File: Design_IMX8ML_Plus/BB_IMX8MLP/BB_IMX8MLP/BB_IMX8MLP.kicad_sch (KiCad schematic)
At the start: 0 parts

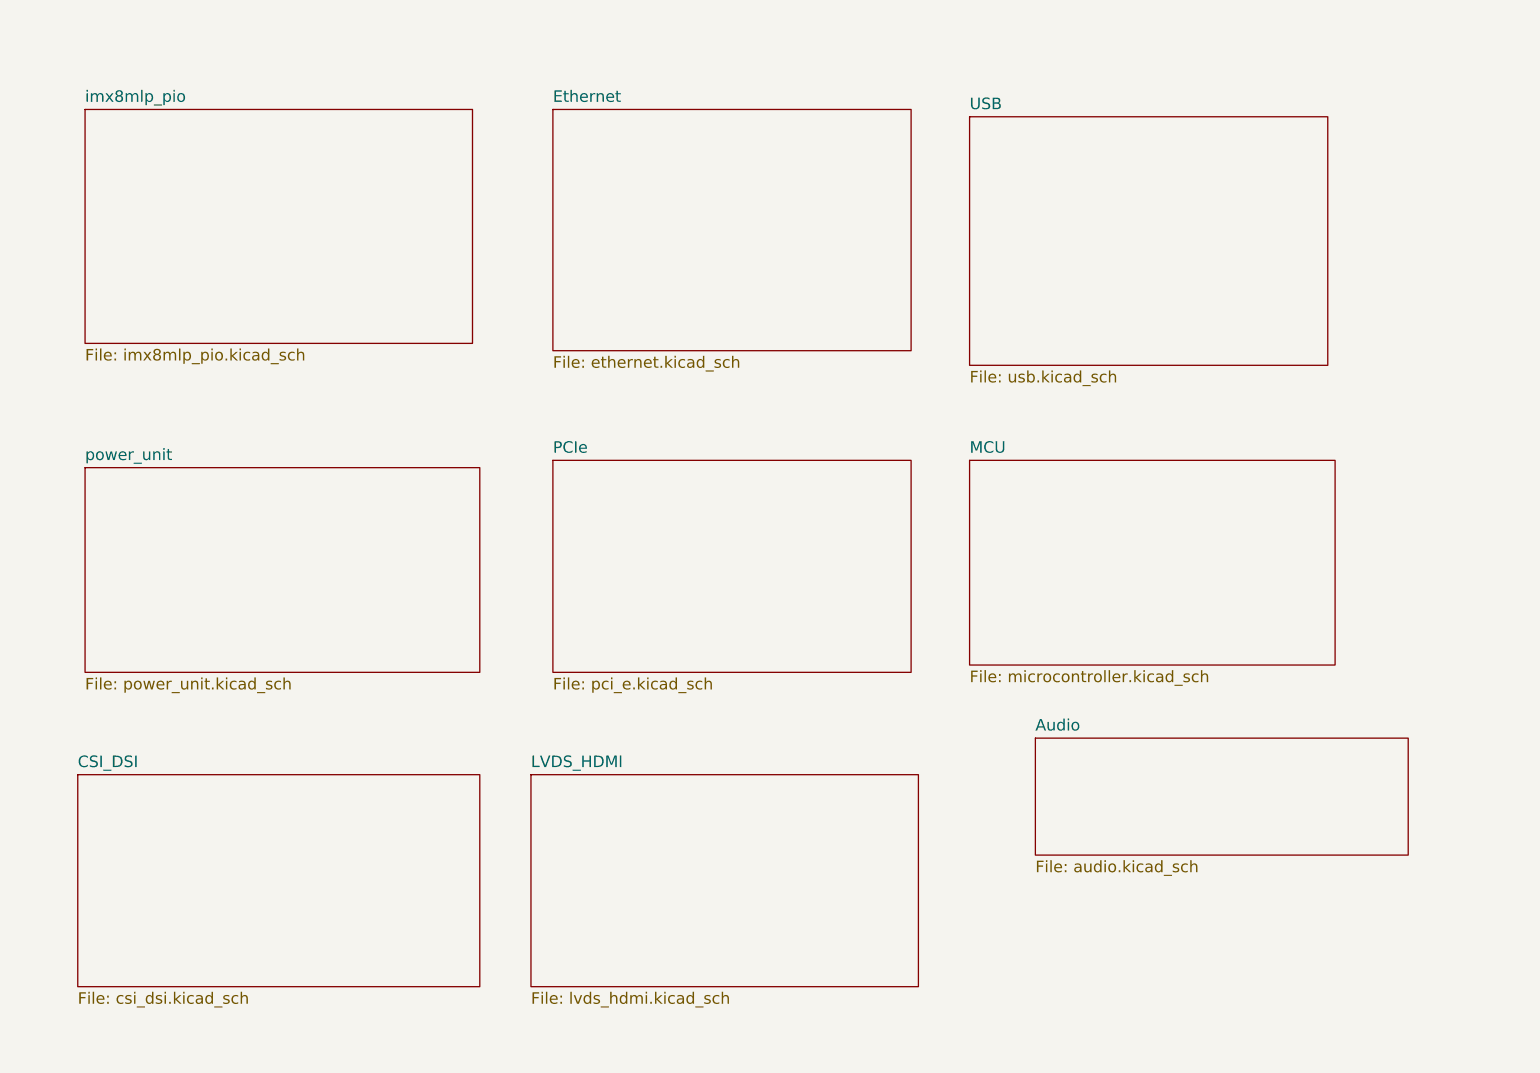
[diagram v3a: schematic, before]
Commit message: Adds audio interface
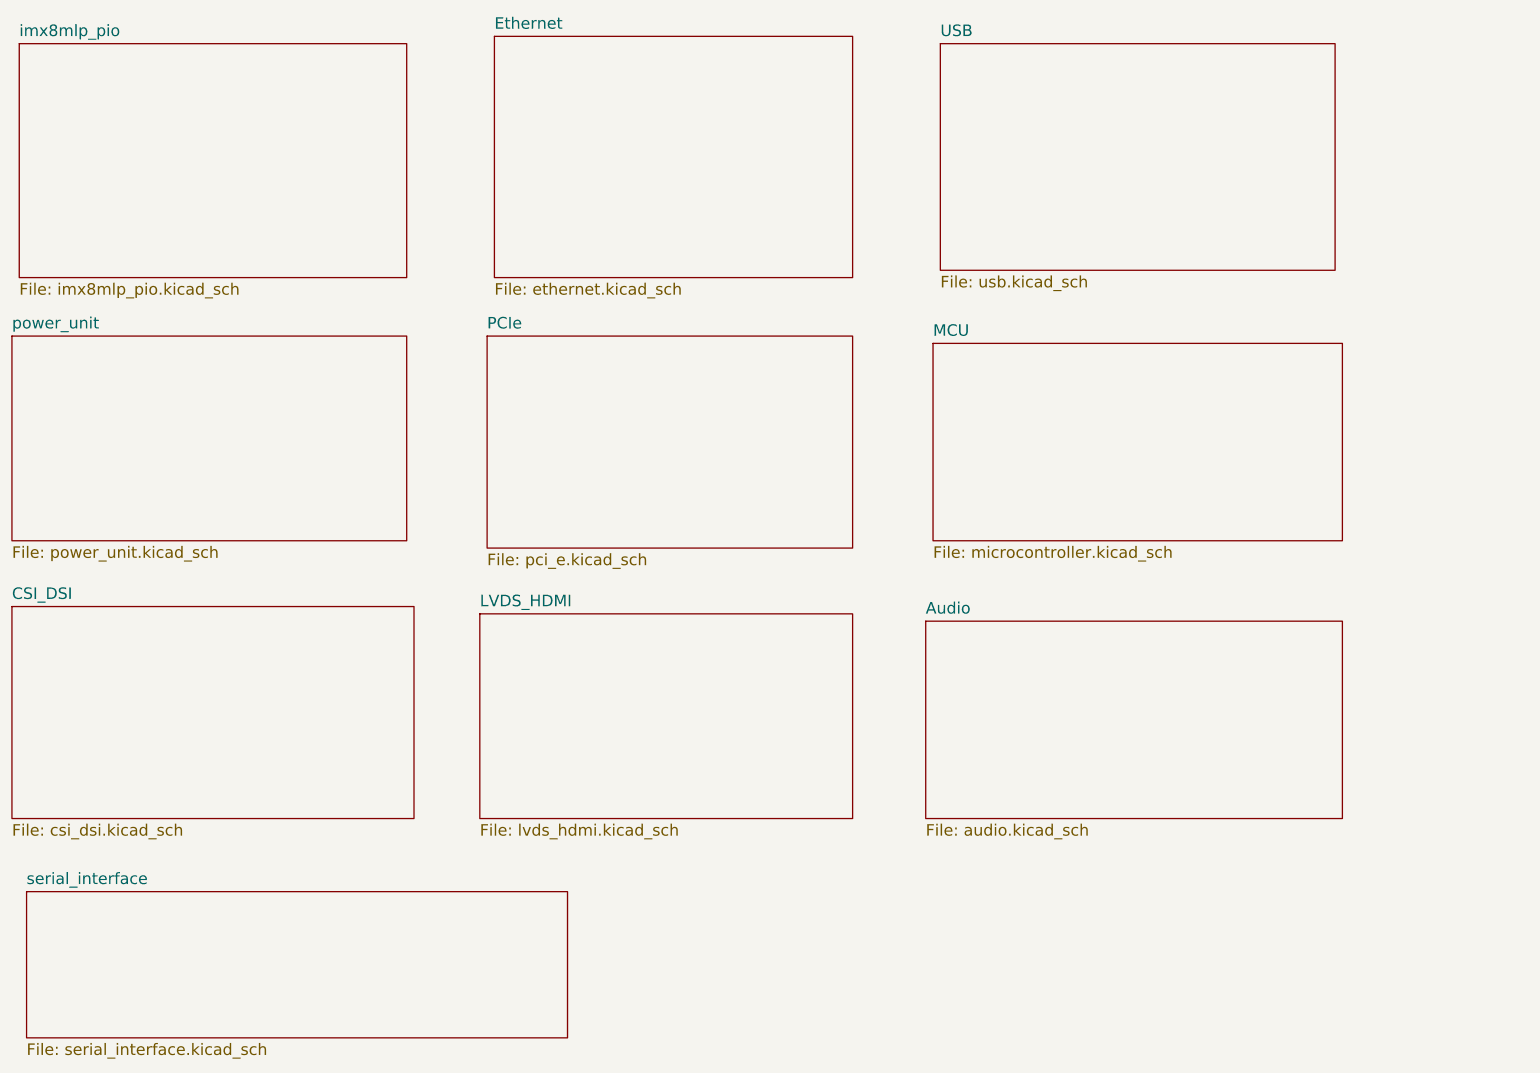
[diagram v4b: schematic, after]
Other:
- added sheet serial_interface (serial_interface.kicad_sch)
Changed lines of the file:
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@@
 	(paper "A4")
 	(sheet
-		(at 111.76 30.48)
+		(at 101.6 17.78)
 		(size 62.23 41.91)
 		(fields_autoplaced yes)
@@
 		)
 		(property "Sheetname" "Ethernet"
-			(at 111.76 29.4034 0)
+			(at 101.6 16.7034 0)
 			(effects
 				(font
@@
 		)
 		(property "Sheetfile" "ethernet.kicad_sch"
-			(at 111.76 73.2666 0)
+			(at 101.6 60.5666 0)
 			(effects
 				(font
@@
 	)
 	(sheet
-		(at 30.48 92.71)
+		(at 17.78 69.85)
 		(size 68.58 35.56)
 		(fields_autoplaced yes)
@@
 		)
 		(property "Sheetname" "power_unit"
-			(at 30.48 91.6334 0)
+			(at 17.78 68.7734 0)
 			(effects
 				(font
@@
 		)
 		(property "Sheetfile" "power_unit.kicad_sch"
-			(at 30.48 129.1466 0)
+			(at 17.78 106.2866 0)
 			(effects
 				(font
@@
 	)
 	(sheet
-		(at 30.48 30.48)
+		(at 20.32 166.37)
+		(size 93.98 25.4)
+		(fields_autoplaced yes)
+		(stroke
+			(width 0.1524)
+			(type solid)
+		)
+		(fill
+			(color 0 0 0 0.0000)
+		)
+		(property "Sheetname" "serial_interface"
+			(at 20.32 165.2934 0)
+			(effects
+				(font
+					(size 2 2)
+				)
+				(justify left bottom)
+			)
+		)
+		(property "Sheetfile" "serial_interface.kicad_sch"
+			(at 20.32 192.6466 0)
+			(effects
+				(font
+					(size 2 2)
+				)
+				(justify left top)
+			)
+		)
+		(instances
+			(project "BB_IMX8MLP"
+				(path "/cd2fb234-91e5-476f-84ed-38419b628dc6"
+					(page "14")
+				)
+			)
+		)
+	)
+	(sheet
+		(at 19.05 19.05)
 		(size 67.31 40.64)
 		(fields_autoplaced yes)
@@
 		)
 		(property "Sheetname" "imx8mlp_pio"
-			(at 30.48 29.4034 0)
+			(at 19.05 17.9734 0)
 			(effects
 				(font
@@
 		)
 		(property "Sheetfile" "imx8mlp_pio.kicad_sch"
-			(at 30.48 71.9966 0)
+			(at 19.05 60.5666 0)
 			(effects
 				(font
@@
 	)
 	(sheet
-		(at 195.58 139.7)
-		(size 64.77 20.32)
+		(at 176.53 119.38)
+		(size 72.39 34.29)
 		(fields_autoplaced yes)
 		(stroke
@@
 		)
 		(property "Sheetname" "Audio"
-			(at 195.58 138.6234 0)
+			(at 176.53 118.3034 0)
 			(effects
 				(font
@@
 		)
 		(property "Sheetfile" "audio.kicad_sch"
-			(at 195.58 160.8966 0)
+			(at 176.53 154.5466 0)
 			(effects
 				(font
@@
 	)
 	(sheet
-		(at 184.15 91.44)
-		(size 63.5 35.56)
+		(at 177.8 71.12)
+		(size 71.12 34.29)
 		(fields_autoplaced yes)
 		(stroke
@@
 		)
 		(property "Sheetname" "MCU"
-			(at 184.15 90.3634 0)
+			(at 177.8 70.0434 0)
 			(effects
 				(font
@@
 		)
 		(property "Sheetfile" "microcontroller.kicad_sch"
-			(at 184.15 127.8766 0)
+			(at 177.8 106.2866 0)
 			(effects
 				(font
@@
 	)
 	(sheet
-		(at 29.21 146.05)
+		(at 17.78 116.84)
 		(size 69.85 36.83)
 		(fields_autoplaced yes)
@@
 		)
 		(property "Sheetname" "CSI_DSI"
-			(at 29.21 144.9734 0)
+			(at 17.78 115.7634 0)
 			(effects
 				(font
@@
 		)
 		(property "Sheetfile" "csi_dsi.kicad_sch"
-			(at 29.21 183.7566 0)
+			(at 17.78 154.5466 0)
 			(effects
 				(font
@@
 	)
 	(sheet
-		(at 184.15 31.75)
-		(size 62.23 43.18)
+		(at 179.07 19.05)
+		(size 68.58 39.37)
 		(fields_autoplaced yes)
 		(stroke
@@
 		)
 		(property "Sheetname" "USB"
-			(at 184.15 30.6734 0)
+			(at 179.07 17.9734 0)
 			(effects
 				(font
@@
 		)
 		(property "Sheetfile" "usb.kicad_sch"
-			(at 184.15 75.8066 0)
+			(at 179.07 59.2966 0)
 			(effects
 				(font
@@
 	)
 	(sheet
-		(at 111.76 91.44)
-		(size 62.23 36.83)
+		(at 100.33 69.85)
+		(size 63.5 36.83)
 		(fields_autoplaced yes)
 		(stroke
@@
 		)
 		(property "Sheetname" "PCIe"
-			(at 111.76 90.3634 0)
+			(at 100.33 68.7734 0)
 			(effects
 				(font
@@
 		)
 		(property "Sheetfile" "pci_e.kicad_sch"
-			(at 111.76 129.1466 0)
+			(at 100.33 107.5566 0)
 			(effects
 				(font
@@
 	)
 	(sheet
-		(at 107.95 146.05)
-		(size 67.31 36.83)
+		(at 99.06 118.11)
+		(size 64.77 35.56)
 		(fields_autoplaced yes)
 		(stroke
@@
 		)
 		(property "Sheetname" "LVDS_HDMI"
-			(at 107.95 144.9734 0)
+			(at 99.06 117.0334 0)
 			(effects
 				(font
@@
 		)
 		(property "Sheetfile" "lvds_hdmi.kicad_sch"
-			(at 107.95 183.7566 0)
-			(effects
-				(font
+			(at 99.06 154.5466 0)
+			(effects
+				(font

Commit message: Review
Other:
- sheet PCIe renamed PCIe_SDCard
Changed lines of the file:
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@@
 			(color 0 0 0 0.0000)
 		)
-		(property "Sheetname" "PCIe"
+		(property "Sheetname" "PCIe_SDCard"
 			(at 100.33 68.7734 0)
 			(effects

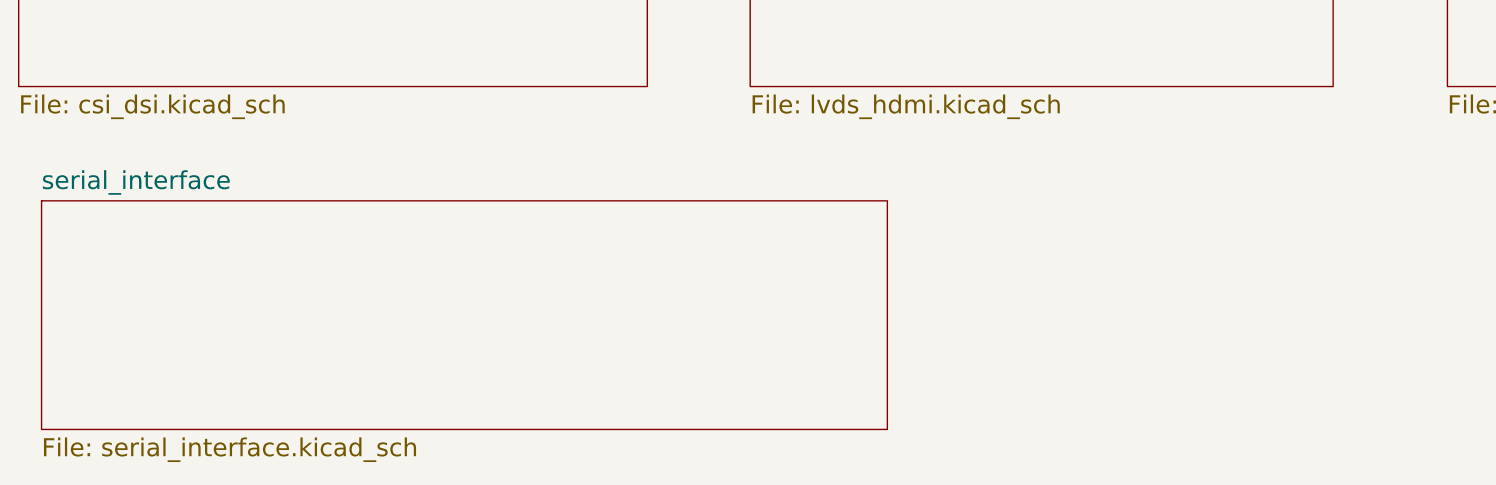
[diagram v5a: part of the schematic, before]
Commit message: reorganization of the componentes
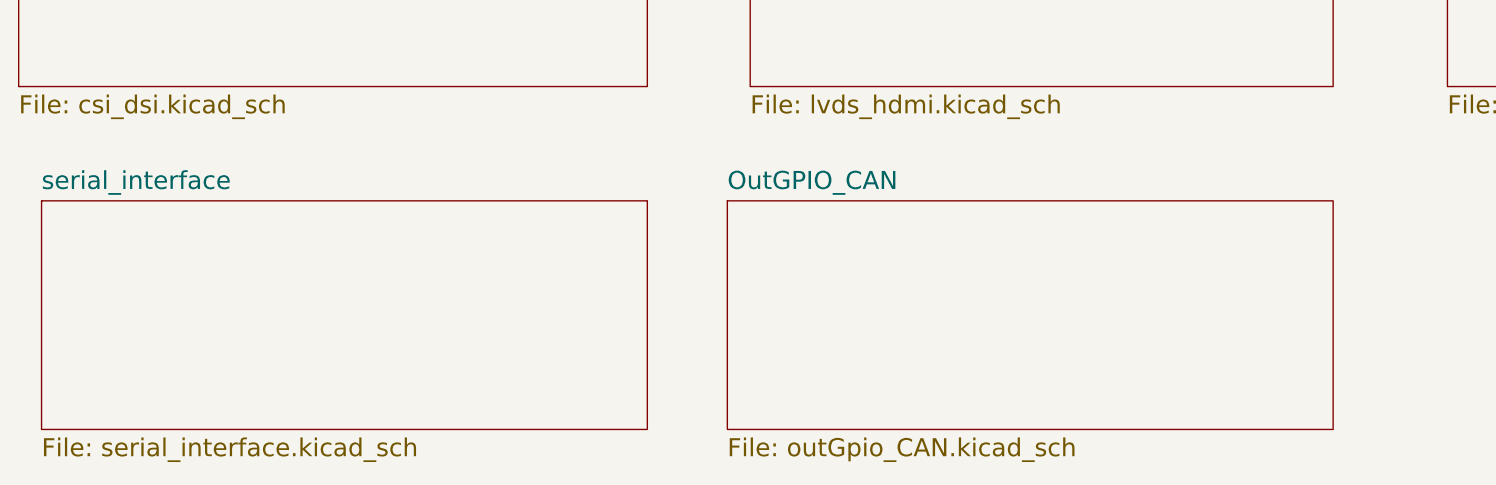
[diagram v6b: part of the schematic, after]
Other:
- added sheet OutGPIO_CAN (outGpio_CAN.kicad_sch)
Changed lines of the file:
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@@
+	)
+	(sheet
+		(at 96.52 166.37)
+		(size 67.31 25.4)
+		(fields_autoplaced yes)
+		(stroke
+			(width 0.1524)
+			(type solid)
+		)
+		(fill
+			(color 0 0 0 0.0000)
+		)
+		(property "Sheetname" "OutGPIO_CAN"
+			(at 96.52 165.2934 0)
+			(effects
+				(font
+					(size 2 2)
+				)
+				(justify left bottom)
+			)
+		)
+		(property "Sheetfile" "outGpio_CAN.kicad_sch"
+			(at 96.52 192.6466 0)
+			(effects
+				(font
+					(size 2 2)
+				)
+				(justify left top)
+			)
+		)
+		(instances
+			(project "BB_IMX8MLP"
+				(path "/cd2fb234-91e5-476f-84ed-38419b628dc6"
+					(page "15")
+				)
+			)
+		)
 	)
 	(sheet
@@
 	(sheet
 		(at 20.32 166.37)
-		(size 93.98 25.4)
+		(size 67.31 25.4)
 		(fields_autoplaced yes)
 		(stroke

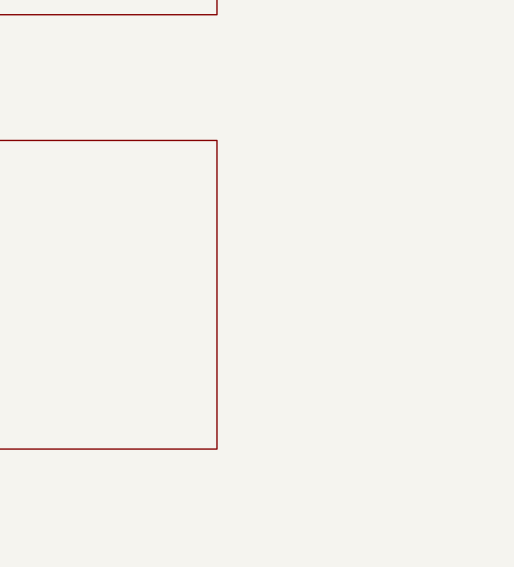
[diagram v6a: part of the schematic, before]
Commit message: Board base resize
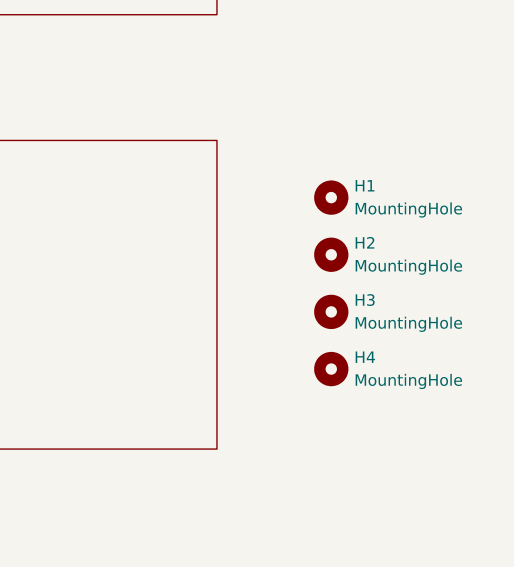
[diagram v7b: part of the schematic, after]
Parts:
- added H1, H2, H3, H4: MountingHole, MountingHole:MountingHole_4.5mm_Pad, symbol Mechanical:MountingHole
